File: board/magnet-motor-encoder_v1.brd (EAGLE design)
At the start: 22 x 22 mm, 12 parts, among them IC1 AS5045B

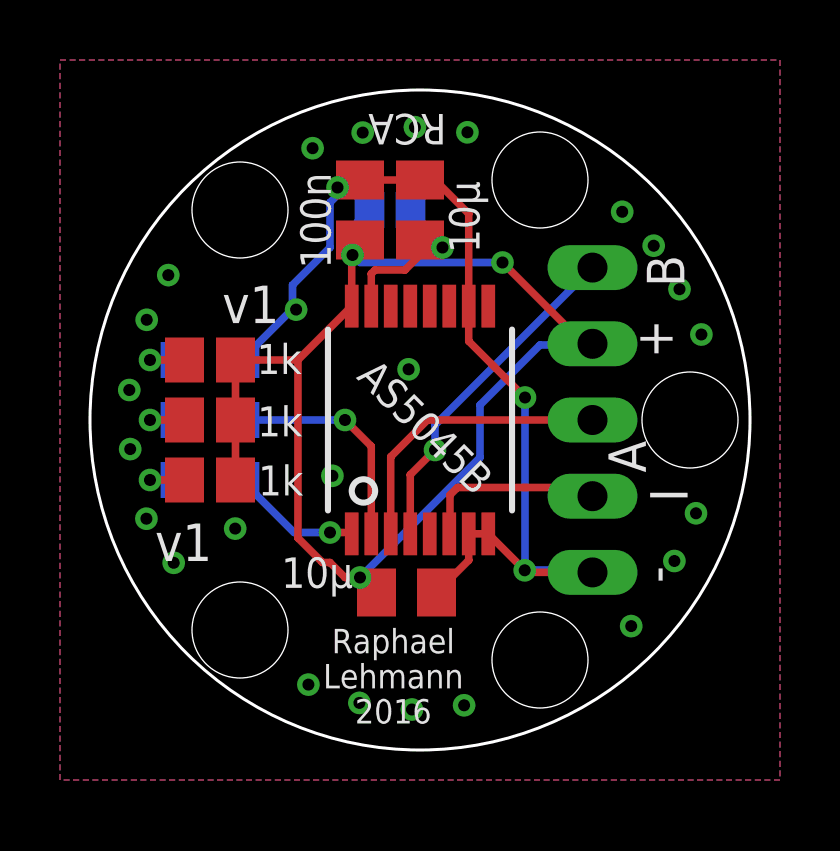
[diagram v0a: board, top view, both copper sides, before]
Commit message: board: add DS18B20 temperature sensor (optional/uses encoder index pin signal)
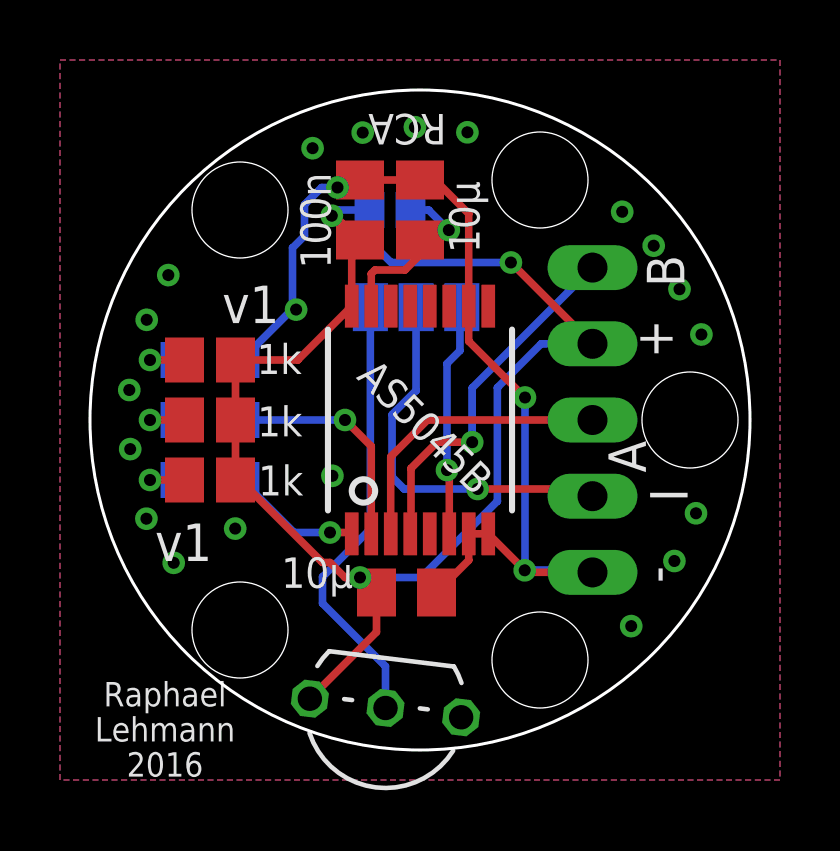
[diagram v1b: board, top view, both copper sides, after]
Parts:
- added IC3: DS18B20, 1wire:TO92-
- added SJ2: (no value), jumper:SJ_2
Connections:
- removed net INDEX: IC1.6, JP1.4
- new net N$1: JP1.4, SJ2.2
- new net N$2: IC1.6, SJ2.1
- new net N$3: IC3.2, SJ2.3
- net +5V: now also IC3.3
- net GND: now also IC3.1
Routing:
- net N$3: track 0.00 -> 14.9 mm
- net N$1: track 0.00 -> 12.9 mm, vias 0 -> 1
- net N$2: track 0.00 -> 7.79 mm, vias 0 -> 1
- net INDEX: track 6.28 -> 0.00 mm
- net +5V: track 43.8 -> 48.0 mm, vias 3 -> 4
- net B: track 11.4 -> 12.1 mm
- net GND: track 34.3 -> 34.6 mm, vias 28 -> 23
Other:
- board text added: "IDX / TMP"
- board text added: "INC DEC POW"
- board text added: "Solder 3V"
- board text removed: "INC DEC POWER"
- board text removed: "Solder"
- board text removed: "for 3V3"

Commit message: board: adjust silk screen; add rev2 label
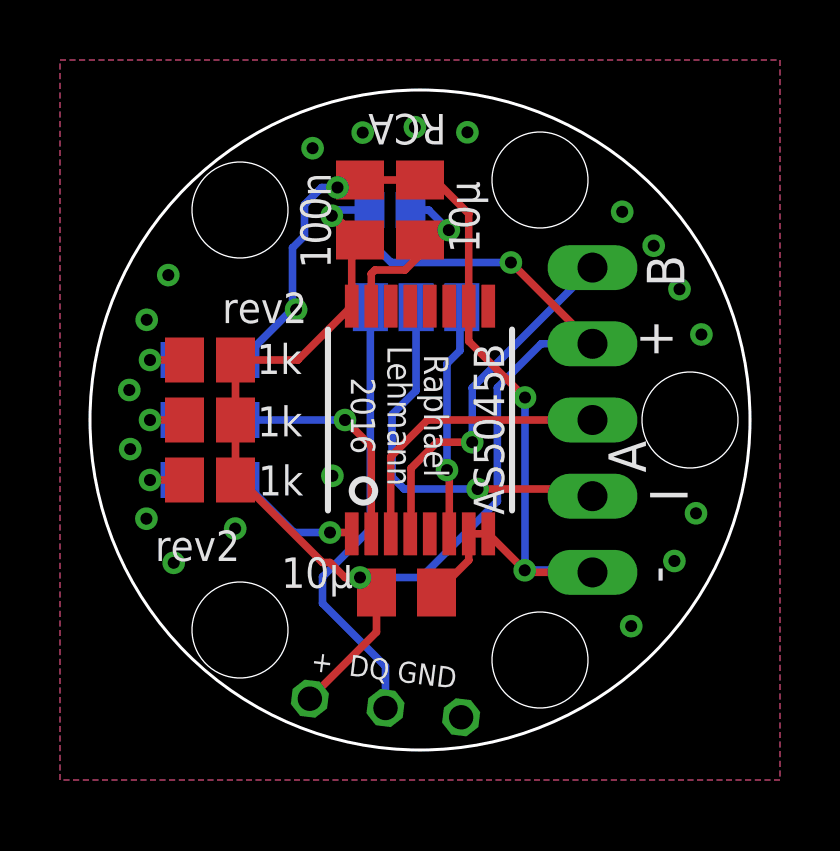
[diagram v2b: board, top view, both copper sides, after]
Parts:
- SJ2: value (none) -> IDX / TEMP
- flipped IC3 to the bottom, turned to 7 degrees
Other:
- board text added: "+ DQ GND"
- board text added: "IDX/TMP"
- board text added: "rev2"
- board text removed: "IDX / TMP"
- board text removed: "v1"
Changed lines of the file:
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@@
 <layer number="14" name="Route14" color="1" fill="6" visible="no" active="no"/>
 <layer number="15" name="Route15" color="4" fill="6" visible="no" active="no"/>
-<layer number="16" name="Bottom" color="1" fill="1" visible="yes" active="yes"/>
+<layer number="16" name="Bottom" color="1" fill="1" visible="no" active="yes"/>
 <layer number="17" name="Pads" color="2" fill="1" visible="yes" active="yes"/>
 <layer number="18" name="Vias" color="2" fill="1" visible="yes" active="yes"/>
@@
 <layer number="20" name="Dimension" color="15" fill="1" visible="yes" active="yes"/>
 <layer number="21" name="tPlace" color="7" fill="1" visible="yes" active="yes"/>
-<layer number="22" name="bPlace" color="7" fill="1" visible="yes" active="yes"/>
+<layer number="22" name="bPlace" color="7" fill="1" visible="no" active="yes"/>
 <layer number="23" name="tOrigins" color="15" fill="1" visible="yes" active="yes"/>
-<layer number="24" name="bOrigins" color="15" fill="1" visible="yes" active="yes"/>
-<layer number="25" name="tNames" color="7" fill="1" visible="no" active="yes"/>
+<layer number="24" name="bOrigins" color="15" fill="1" visible="no" active="yes"/>
+<layer number="25" name="tNames" color="7" fill="1" visible="yes" active="yes"/>
 <layer number="26" name="bNames" color="7" fill="1" visible="no" active="yes"/>
-<layer number="27" name="tValues" color="7" fill="1" visible="no" active="yes"/>
+<layer number="27" name="tValues" color="7" fill="1" visible="yes" active="yes"/>
 <layer number="28" name="bValues" color="7" fill="1" visible="no" active="yes"/>
 <layer number="29" name="tStop" color="7" fill="3" visible="no" active="yes"/>
@@
 <layer number="41" name="tRestrict" color="4" fill="10" visible="no" active="yes"/>
 <layer number="42" name="bRestrict" color="1" fill="10" visible="no" active="yes"/>
-<layer number="43" name="vRestrict" color="2" fill="10" visible="yes" active="yes"/>
+<layer number="43" name="vRestrict" color="2" fill="10" visible="no" active="yes"/>
 <layer number="44" name="Drills" color="7" fill="1" visible="no" active="yes"/>
-<layer number="45" name="Holes" color="7" fill="1" visible="yes" active="yes"/>
+<layer number="45" name="Holes" color="7" fill="1" visible="no" active="yes"/>
 <layer number="46" name="Milling" color="3" fill="1" visible="no" active="yes"/>
 <layer number="47" name="Measures" color="7" fill="1" visible="no" active="yes"/>
 <layer number="48" name="Document" color="7" fill="1" visible="no" active="yes"/>
-<layer number="49" name="Reference" color="7" fill="1" visible="yes" active="yes"/>
+<layer number="49" name="Reference" color="7" fill="1" visible="no" active="yes"/>
 <layer number="50" name="dxf" color="7" fill="1" visible="no" active="no"/>
 <layer number="51" name="tDocu" color="7" fill="1" visible="no" active="yes"/>
@@
 <hole x="4" y="8" drill="3.2"/>
 <text x="1.52" y="7.96" size="0.8128" layer="26" rot="MR0">Solder 3V</text>
-<text x="1.13" y="0.94" size="0.9" layer="26" rot="SMR270">LEDs 2mA</text>
-<text x="-5.11" y="-3.57" size="0.7" layer="26" rot="MR0">YELLOW</text>
+<text x="1.14" y="1.65" size="0.9" layer="26" rot="SMR270">LEDs 2mA</text>
+<text x="-5.11" y="-3.57" size="0.8" layer="26" rot="MR0">YELLOW</text>
 <text x="-8.94" y="1.08" size="0.8" layer="26" rot="MR270">RED</text>
 <text x="-5.77" y="2.83" size="0.8" layer="26" rot="MR0">BLUE</text>
@@
 <text x="4.25" y="-4.72" size="1.25" layer="26" rot="MR270">-</text>
 <text x="4.12" y="5.57" size="1.25" layer="26" rot="SMR270">B</text>
-<text x="-5.37" y="2.94" size="1.4224" layer="26" ratio="15" rot="SMR180">INC
+<text x="-5.16" y="2.65" size="1.4224" layer="26" ratio="15" rot="SMR180">INC
 DEC
 POW</text>
-<text x="2.17" y="0.9" size="0.9" layer="26" rot="SMR270">low current</text>
-<text x="-8.5" y="-10.31" size="0.8128" layer="25" ratio="15" distance="44" align="center">Raphael
-Lehmann
-2016</text>
-<text x="-8.83" y="-4.7" size="1.25" layer="25" ratio="15" distance="44">v1</text>
-<text x="-6.59" y="3.23" size="1.25" layer="25" ratio="15" distance="44">v1</text>
-<text x="-7.21" y="-4.87" size="1.25" layer="26" ratio="15" distance="44" rot="MR0">v1</text>
-<text x="-0.92" y="-6.96" size="0.8128" layer="26" ratio="15" distance="44" rot="MR0" align="center">Magnet
+<text x="2.22" y="1.65" size="0.9" layer="26" rot="SMR270">low current</text>
+<text x="-8.83" y="-4.7" size="1.016" layer="25" ratio="15" distance="44">rev2</text>
+<text x="-6.59" y="3.23" size="1.016" layer="25" ratio="15" distance="44">rev2</text>
+<text x="-4.69" y="-4.95" size="1.016" layer="26" ratio="15" distance="44" rot="MR0">rev2</text>
+<text x="-1.77" y="-4.98" size="0.9" layer="26" ratio="15" distance="44" rot="SMR0" align="center">Magnet
 Motor
 Encoder</text>
@@
 <text x="-8.03" y="0.59" size="1.016" layer="26" ratio="15" distance="44" rot="MR0">+</text>
 <text x="-8.02" y="-1.41" size="1.016" layer="26" ratio="15" distance="44" rot="MR0">+</text>
-<text x="2.27" y="4.88" size="0.8128" layer="26" rot="SMR0">IDX / TMP</text>
+<text x="2.27" y="4.88" size="0.8128" layer="26" rot="SMR0">IDX/TMP</text>
+<text x="-0.68" y="0.14" size="0.8128" layer="25" rot="SR270" align="center">Raphael
+Lehmann
+2016</text>
+<text x="-4.61" y="3.98" size="1.016" layer="26" ratio="15" distance="44" rot="MR0">rev2</text>
+<text x="-3.66" y="-8.36" size="0.7" layer="25" font="vector" rot="SR353">+  DQ GND</text>
 </plain>
 <attributes>
@@
 <attribute name="MF" value="" x="16.51" y="-5.08" size="1.778" layer="27" display="off"/>
 <attribute name="OC_FARNELL" value="1630800" x="16.51" y="-5.08" size="1.778" layer="27" display="off"/>
-<attribute name="VALUE" x="2.53" y="-1.855" size="1" layer="25" rot="R135"/>
+<attribute name="VALUE" x="2.805" y="-3.16" size="1.016" layer="25" rot="SR90"/>
 </element>
 <element name="LED_YELLOW" library="led" package="CHIPLED_0805" value="INC" x="-7" y="-2" smashed="yes" rot="MR90"/>
@@
 <attribute name="VALUE" x="10.83" y="6.35" size="1.016" layer="28" ratio="10" rot="MR270"/>
 </element>
-<element name="SJ2" library="jumper" package="SJ_2" value="" x="-0.13" y="3.76" smashed="yes" rot="MR0">
+<element name="SJ2" library="jumper" package="SJ_2" value="IDX / TEMP" x="-0.13" y="3.76" smashed="yes" rot="MR0">
 <attribute name="VALUE" x="-0.0299" y="3.76" size="0.02" layer="28" rot="MR0"/>
 </element>
-<element name="IC3" library="1wire" package="TO92-" value="DS18B20" x="-1.15" y="-9.6" smashed="yes" rot="R173">
-<attribute name="VALUE" x="0.853478125" y="-8.422159375" size="0.6096" layer="27" ratio="10" rot="R173"/>
+<element name="IC3" library="1wire" package="TO92-" value="DS18B20" x="-1.15" y="-9.6" smashed="yes" rot="MR7">
+<attribute name="VALUE" x="0.69901875" y="-8.8275375" size="0.6096" layer="26" ratio="10" rot="MR7"/>
 </element>
 </elements>
@@
 <wire x1="-3.25" y1="-4.75" x2="-6" y2="-2" width="0.254" layer="1"/>
 <wire x1="-6" y1="-2" x2="-6.15" y2="-2" width="0.254" layer="1"/>
-<wire x1="-1.45" y1="-5.75" x2="-1.45" y2="-7.069384375" width="0.254" layer="1"/>
-<wire x1="-1.45" y1="-7.069384375" x2="-3.671065625" y2="-9.29045" width="0.254" layer="1"/>
 <wire x1="4.04" y1="2.54" x2="2.58" y2="1.08" width="0.254" layer="16"/>
 <wire x1="2.58" y1="1.08" x2="2.58" y2="-2.71" width="0.254" layer="16"/>
@@
 <wire x1="-1.7427" y1="6.94" x2="-1.7427" y2="6.0327" width="0.254" layer="16"/>
 <wire x1="-1.7427" y1="6.0327" x2="-0.96" y2="5.25" width="0.254" layer="16"/>
-<wire x1="-0.96" y1="5.25" x2="2.72" y2="5.25" width="0.254" layer="16"/>
-<wire x1="2.72" y1="5.25" x2="2.75" y2="5.25" width="0.254" layer="16"/>
+<wire x1="-0.96" y1="5.25" x2="3.03" y2="5.25" width="0.254" layer="16"/>
 <wire x1="-2" y1="5.97" x2="-2.84" y2="6.81" width="0.254" layer="1"/>
 <wire x1="-2.84" y1="6.81" x2="-2.94" y2="6.81" width="0.254" layer="1"/>
@@
 <wire x1="5.74" y1="2.54" x2="3.03" y2="5.25" width="0.254" layer="1"/>
 <via x="3.03" y="5.25" extent="1-16" drill="0.4"/>
-<wire x1="3.03" y1="5.25" x2="2.75" y2="5.25" width="0.254" layer="16"/>
+<wire x1="-1.45" y1="-5.75" x2="-1.45" y2="-7.069384375" width="0.254" layer="1"/>
+<wire x1="-1.45" y1="-7.069384375" x2="-3.671065625" y2="-9.29045" width="0.254" layer="1"/>
 </signal>
 <signal name="+3V3">
@@
 <contactref element="IC3" pad="2"/>
 <contactref element="SJ2" pad="3"/>
-<wire x1="-1.15" y1="-9.6" x2="-1.15" y2="-8.21" width="0.254" layer="16"/>
-<wire x1="-1.15" y1="-8.21" x2="-3.25" y2="-6.11" width="0.254" layer="16"/>
 <wire x1="-3.25" y1="-6.11" x2="-3.25" y2="-5.23" width="0.254" layer="16"/>
 <wire x1="-3.25" y1="-5.23" x2="-1.654" y2="-3.634" width="0.254" layer="16"/>
 <wire x1="-1.654" y1="-3.634" x2="-1.654" y2="3.76" width="0.254" layer="16"/>
+<wire x1="-1.15" y1="-9.6" x2="-1.15" y2="-8.21" width="0.254" layer="16"/>
+<wire x1="-1.15" y1="-8.21" x2="-3.25" y2="-6.11" width="0.254" layer="16"/>
 </signal>
 </signals>

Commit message: board: some minor fixes and improvements; rev3 label
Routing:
- net N$1: track 12.9 -> 11.7 mm
- net +5V: vias 4 -> 3
- net GND: vias 23 -> 24
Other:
- board text added: "rev3"
- board text removed: "rev2"
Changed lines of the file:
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@@
 <grid distance="0.01" unitdist="mm" unit="mm" style="dots" multiple="1" display="yes" altdistance="0.02" altunitdist="mm" altunit="mm"/>
 <layers>
-<layer number="1" name="Top" color="4" fill="1" visible="yes" active="yes"/>
+<layer number="1" name="Top" color="4" fill="1" visible="no" active="yes"/>
 <layer number="2" name="Route2" color="1" fill="3" visible="no" active="no"/>
 <layer number="3" name="Route3" color="4" fill="3" visible="no" active="no"/>
@@
 <layer number="14" name="Route14" color="1" fill="6" visible="no" active="no"/>
 <layer number="15" name="Route15" color="4" fill="6" visible="no" active="no"/>
-<layer number="16" name="Bottom" color="1" fill="1" visible="no" active="yes"/>
+<layer number="16" name="Bottom" color="1" fill="1" visible="yes" active="yes"/>
 <layer number="17" name="Pads" color="2" fill="1" visible="yes" active="yes"/>
 <layer number="18" name="Vias" color="2" fill="1" visible="yes" active="yes"/>
 <layer number="19" name="Unrouted" color="6" fill="1" visible="yes" active="yes"/>
 <layer number="20" name="Dimension" color="15" fill="1" visible="yes" active="yes"/>
-<layer number="21" name="tPlace" color="7" fill="1" visible="yes" active="yes"/>
-<layer number="22" name="bPlace" color="7" fill="1" visible="no" active="yes"/>
-<layer number="23" name="tOrigins" color="15" fill="1" visible="yes" active="yes"/>
-<layer number="24" name="bOrigins" color="15" fill="1" visible="no" active="yes"/>
-<layer number="25" name="tNames" color="7" fill="1" visible="yes" active="yes"/>
-<layer number="26" name="bNames" color="7" fill="1" visible="no" active="yes"/>
-<layer number="27" name="tValues" color="7" fill="1" visible="yes" active="yes"/>
-<layer number="28" name="bValues" color="7" fill="1" visible="no" active="yes"/>
+<layer number="21" name="tPlace" color="7" fill="1" visible="no" active="yes"/>
+<layer number="22" name="bPlace" color="7" fill="1" visible="yes" active="yes"/>
+<layer number="23" name="tOrigins" color="15" fill="1" visible="no" active="yes"/>
+<layer number="24" name="bOrigins" color="15" fill="1" visible="yes" active="yes"/>
+<layer number="25" name="tNames" color="7" fill="1" visible="no" active="yes"/>
+<layer number="26" name="bNames" color="7" fill="1" visible="yes" active="yes"/>
+<layer number="27" name="tValues" color="7" fill="1" visible="no" active="yes"/>
+<layer number="28" name="bValues" color="7" fill="1" visible="yes" active="yes"/>
 <layer number="29" name="tStop" color="7" fill="3" visible="no" active="yes"/>
 <layer number="30" name="bStop" color="7" fill="6" visible="no" active="yes"/>
@@
 POW</text>
 <text x="2.22" y="1.65" size="0.9" layer="26" rot="SMR270">low current</text>
-<text x="-8.83" y="-4.7" size="1.016" layer="25" ratio="15" distance="44">rev2</text>
-<text x="-6.59" y="3.23" size="1.016" layer="25" ratio="15" distance="44">rev2</text>
-<text x="-4.69" y="-4.95" size="1.016" layer="26" ratio="15" distance="44" rot="MR0">rev2</text>
+<text x="-8.83" y="-4.7" size="1.016" layer="25" ratio="15" distance="44">rev3</text>
+<text x="-6.59" y="3.23" size="1.016" layer="25" ratio="15" distance="44">rev3</text>
+<text x="-4.69" y="-4.95" size="1.016" layer="26" ratio="15" distance="44" rot="MR0">rev3</text>
 <text x="-1.77" y="-4.98" size="0.9" layer="26" ratio="15" distance="44" rot="SMR0" align="center">Magnet
 Motor
@@
 Lehmann
 2016</text>
-<text x="-4.61" y="3.98" size="1.016" layer="26" ratio="15" distance="44" rot="MR0">rev2</text>
+<text x="-4.61" y="3.98" size="1.016" layer="26" ratio="15" distance="44" rot="MR0">rev3</text>
 <text x="-3.66" y="-8.36" size="0.7" layer="25" font="vector" rot="SR353">+  DQ GND</text>
 </plain>
@@
 <wire x1="-2.94" y1="6.81" x2="-2.75" y2="7" width="0.254" layer="16"/>
 <wire x1="-2.75" y1="7" x2="-1.6827" y2="7" width="0.254" layer="16"/>
-<wire x1="4.04" y1="2.54" x2="5.74" y2="2.54" width="0.254" layer="16"/>
-<via x="5.74" y="2.54" extent="1-16" drill="0.4"/>
-<wire x1="5.74" y1="2.54" x2="5.75" y2="2.54" width="0.254" layer="16"/>
-<wire x1="5.74" y1="2.54" x2="3.03" y2="5.25" width="0.254" layer="1"/>
 <via x="3.03" y="5.25" extent="1-16" drill="0.4"/>
 <wire x1="-1.45" y1="-5.75" x2="-1.45" y2="-7.069384375" width="0.254" layer="1"/>
 <wire x1="-1.45" y1="-7.069384375" x2="-3.671065625" y2="-9.29045" width="0.254" layer="1"/>
+<wire x1="5.75" y1="2.54" x2="5.74" y2="2.54" width="0.254" layer="1"/>
+<wire x1="5.74" y1="2.54" x2="3.03" y2="5.25" width="0.254" layer="1"/>
+<wire x1="5.75" y1="2.54" x2="4.04" y2="2.54" width="0.254" layer="16"/>
 </signal>
 <signal name="+3V3">
@@
 <wire x1="-3.85" y1="7.18" x2="-3.28" y2="7.75" width="0.254" layer="16"/>
 <wire x1="-3.28" y1="7.75" x2="-2.75" y2="7.75" width="0.254" layer="16"/>
+<via x="-0.89" y="0.81" extent="1-16" drill="0.4"/>
 </signal>
 <signal name="A">
@@
 <contactref element="JP1" pad="4"/>
 <via x="1.92" y="-2.3" extent="1-16" drill="0.4"/>
-<wire x1="-0.53" y1="-2.3" x2="1.92" y2="-2.3" width="0.254" layer="16"/>
 <wire x1="1.92" y1="-2.3" x2="5.51" y2="-2.3" width="0.254" layer="1"/>
 <wire x1="5.51" y1="-2.3" x2="5.75" y2="-2.54" width="0.254" layer="1"/>
-<wire x1="-0.13" y1="3.76" x2="-0.13" y2="0.98" width="0.254" layer="16"/>
-<wire x1="-0.13" y1="0.98" x2="-0.93" y2="0.18" width="0.254" layer="16"/>
-<wire x1="-0.93" y1="0.18" x2="-0.93" y2="-1.9" width="0.254" layer="16"/>
-<wire x1="-0.93" y1="-1.9" x2="-0.53" y2="-2.3" width="0.254" layer="16"/>
+<wire x1="-0.13" y1="3.76" x2="-0.13" y2="-1.66" width="0.254" layer="16"/>
+<wire x1="-0.13" y1="-1.66" x2="0.51" y2="-2.3" width="0.254" layer="16"/>
+<wire x1="0.51" y1="-2.3" x2="1.92" y2="-2.3" width="0.254" layer="16"/>
 </signal>
 <signal name="N$2">
